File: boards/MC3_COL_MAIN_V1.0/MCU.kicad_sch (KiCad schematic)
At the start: 39 parts, among them J2 SWD, SW1 SKRKAEE020, U10 GP1S094HCZ0F, U2 STM32F412RET6, U9 AEDR-8300-1Q0, Y1 8MHz

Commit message: GP1S094 from datasheet: pins 1=A 2=C 3=E 4=K, THT footprint (4.55x2.0 grid, 1.2mm boss NPTH); R36->100R R37->47k for worst-case CTR; ref collisions fixed (C33->C37, #PWR010-013->#PWR0107-0110)
Co-Authored-By: Claude Fable 5 <noreply@anthropic.com>
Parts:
- R36: value 220R -> 100R; LCSC C25091 -> C25076; Note no COTS record - commodity support part; ~10 mA IR LED from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 -> no COTS record - IR LED drive ~20 mA from +3V3; sized again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
- R37: value 10k -> 47k; LCSC C25744 -> C25792; Note no COTS record - phototransistor pull-up to +3V3 -> no COTS record - collector pull-up sized for worst-case CTR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
- U10: footprint (none) -> MC3_COL_MAIN:GP1S094HCZ0F; Note PROVISIONAL - yaw homing datum, transmissive interrupter, 3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 -> Yaw homing datum, 3 mm slot 0.3 mm aperture. Flag present =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
- renumbered C33 to C37
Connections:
- net GND: now also U10.3 (E); no longer U10.2 (K)
- net YAW_HOME: now also U10.2 (C); no longer U10.3 (C)

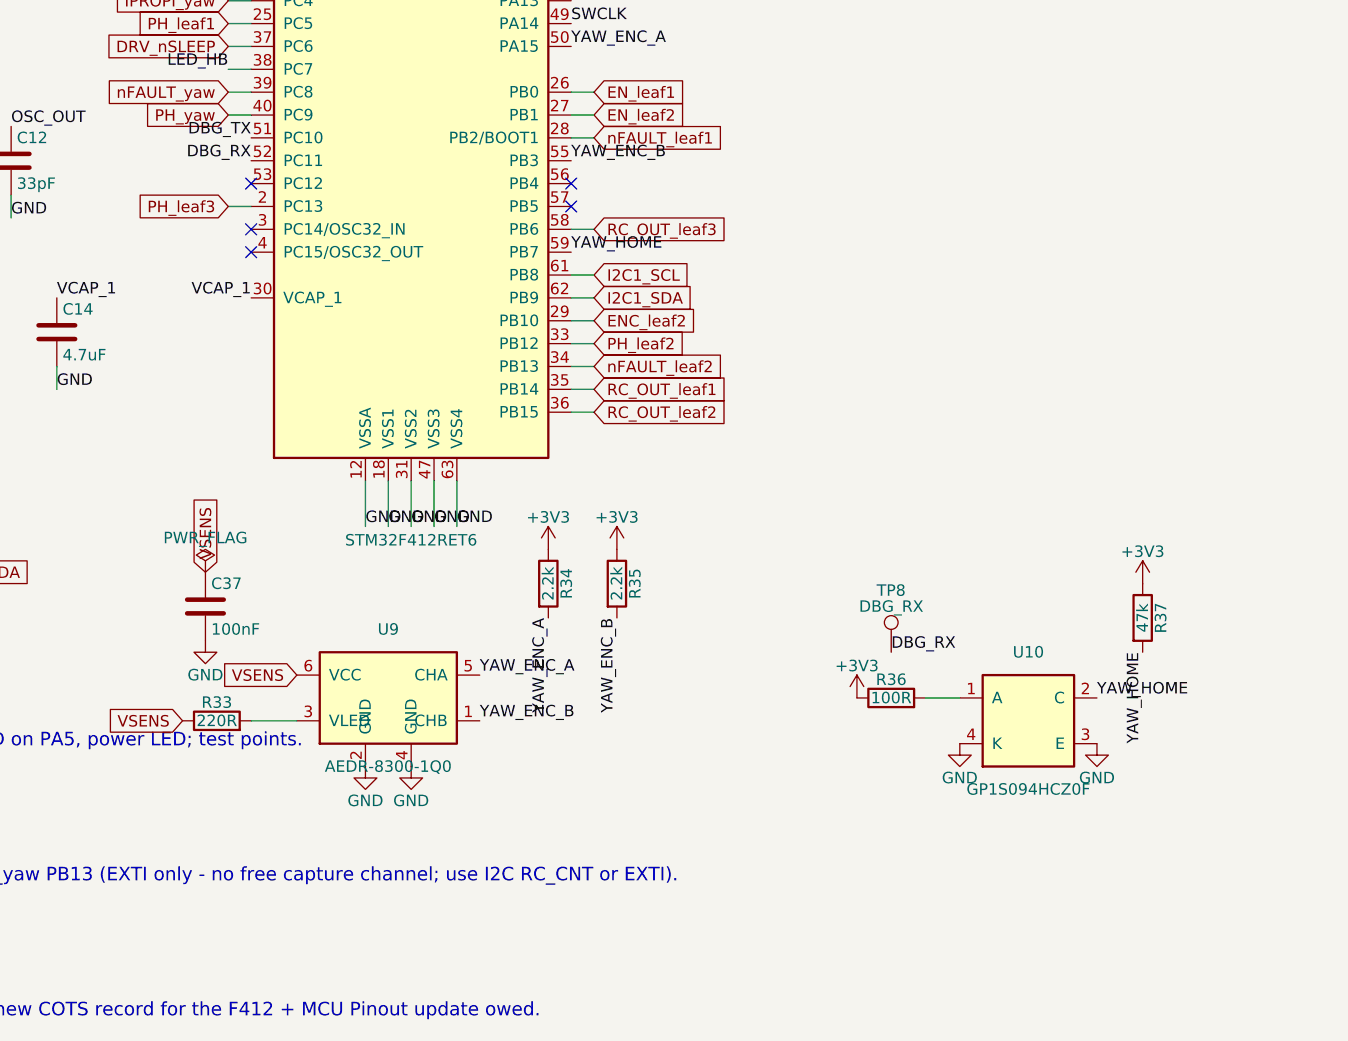
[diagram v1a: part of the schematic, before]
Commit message: Second yaw interrupter U11 (+R38/R39): YAW_LIM on PC12/EXTI, 180 deg from U10 - both hard stops get soft limits; power refs pre-renamed #PWR0111-0114
Co-Authored-By: Claude Fable 5 <noreply@anthropic.com>
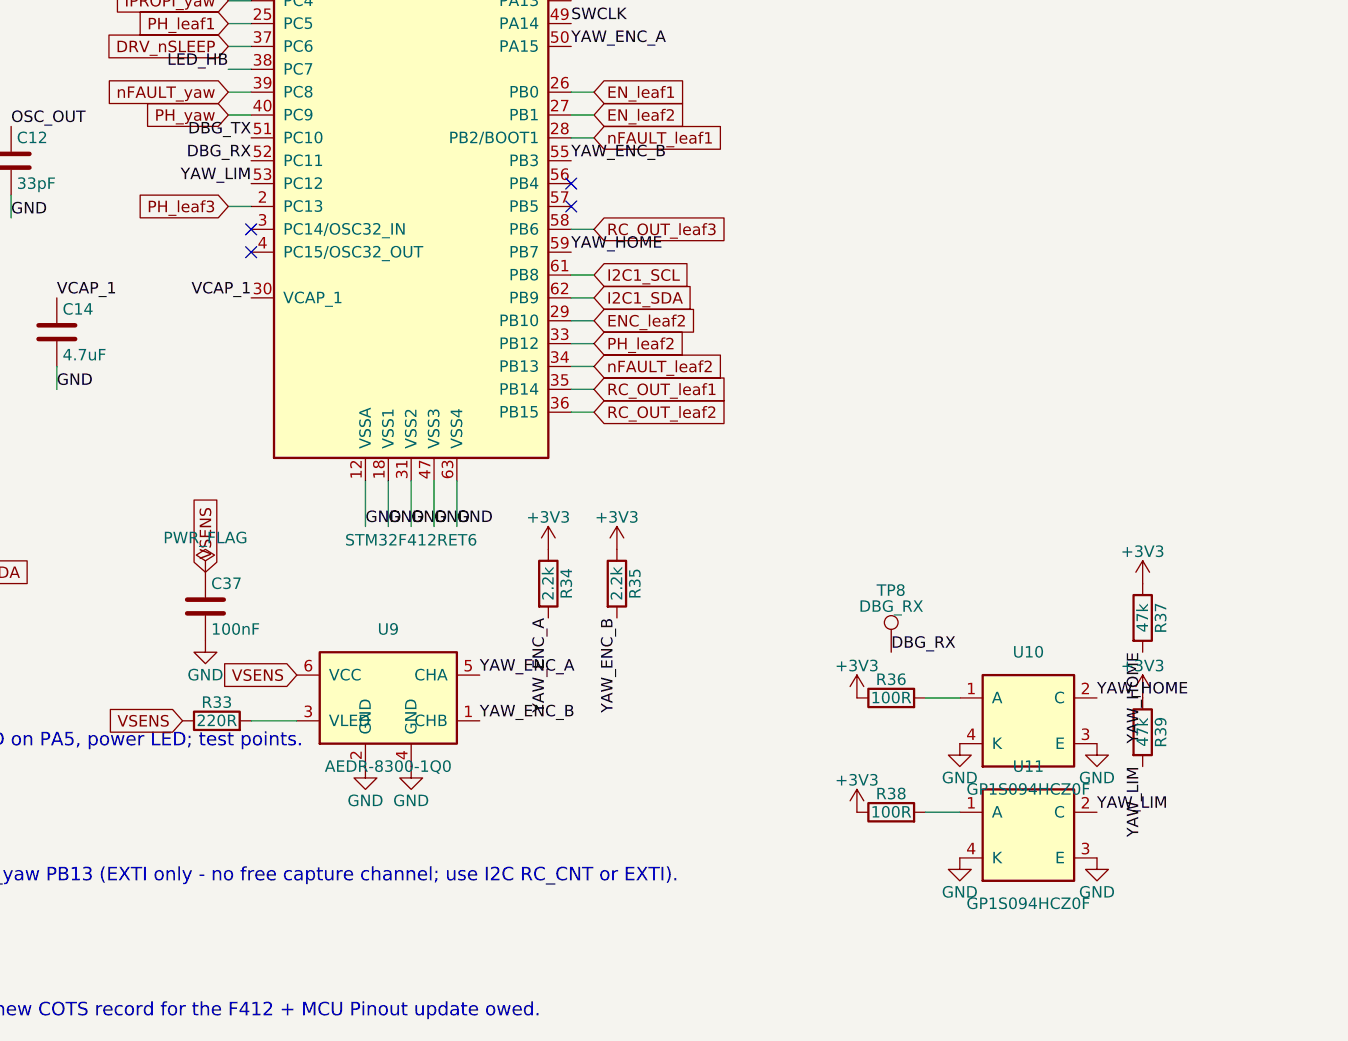
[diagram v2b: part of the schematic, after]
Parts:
- added R38: 100R, MC3_COL_MAIN:R_0402_1005Metric, symbol Device:R
- added R39: 47k, MC3_COL_MAIN:R_0402_1005Metric, symbol Device:R
- added U11: GP1S094HCZ0F, MC3_COL_MAIN:GP1S094HCZ0F, symbol MC3_COL_MAIN:GP1S094HCZ0F
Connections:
- net +3V3: now also R38.1, R39.1
- net GND: now also U11.3 (E), U11.4 (K)
- net YAW_LIM: now reaches U2.53 (PC12)
- net YAW_LIM: now also R39.2, U11.2 (C)
- new net: R38.2, U11.1 (A)
- no-connect marks 6 -> 5

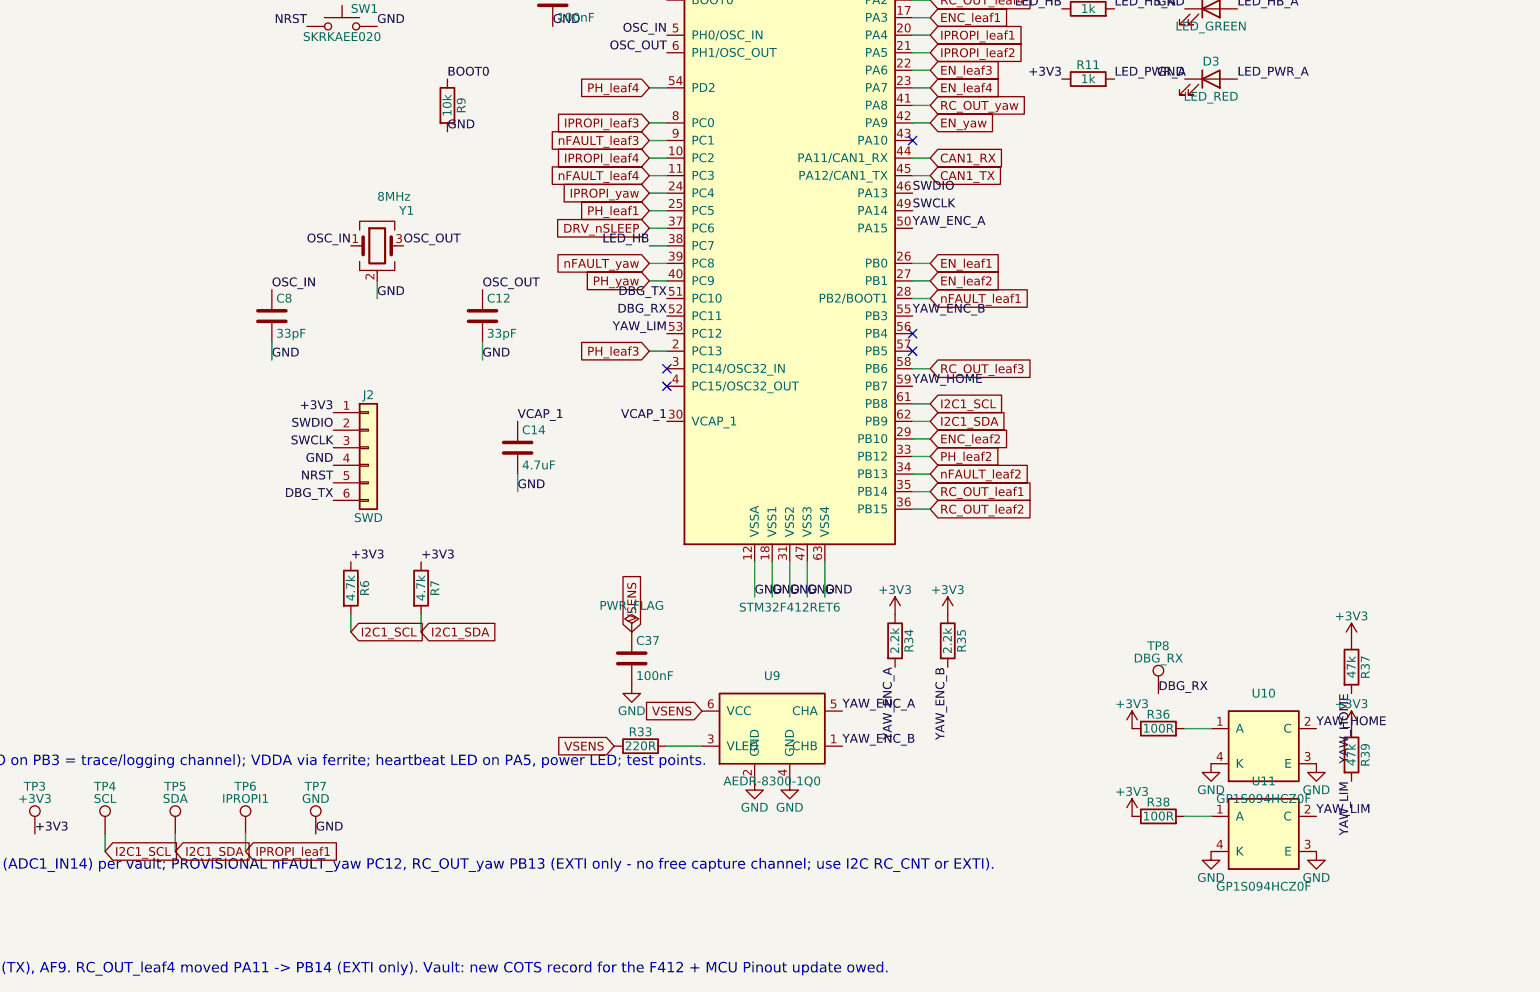
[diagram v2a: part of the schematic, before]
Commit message: Review fixes applied (C21, C37 order, stitching vias) + review-driven adds: 5x 1nF IPROPI ADC filters (C38-42, C1523), U8 VIO 100nF (C43), 3x M2.5 NPTH mounting holes (H1-3) - caps placed unwired, user wires; holes placed in layout by user
Co-Authored-By: Claude Fable 5 <noreply@anthropic.com>
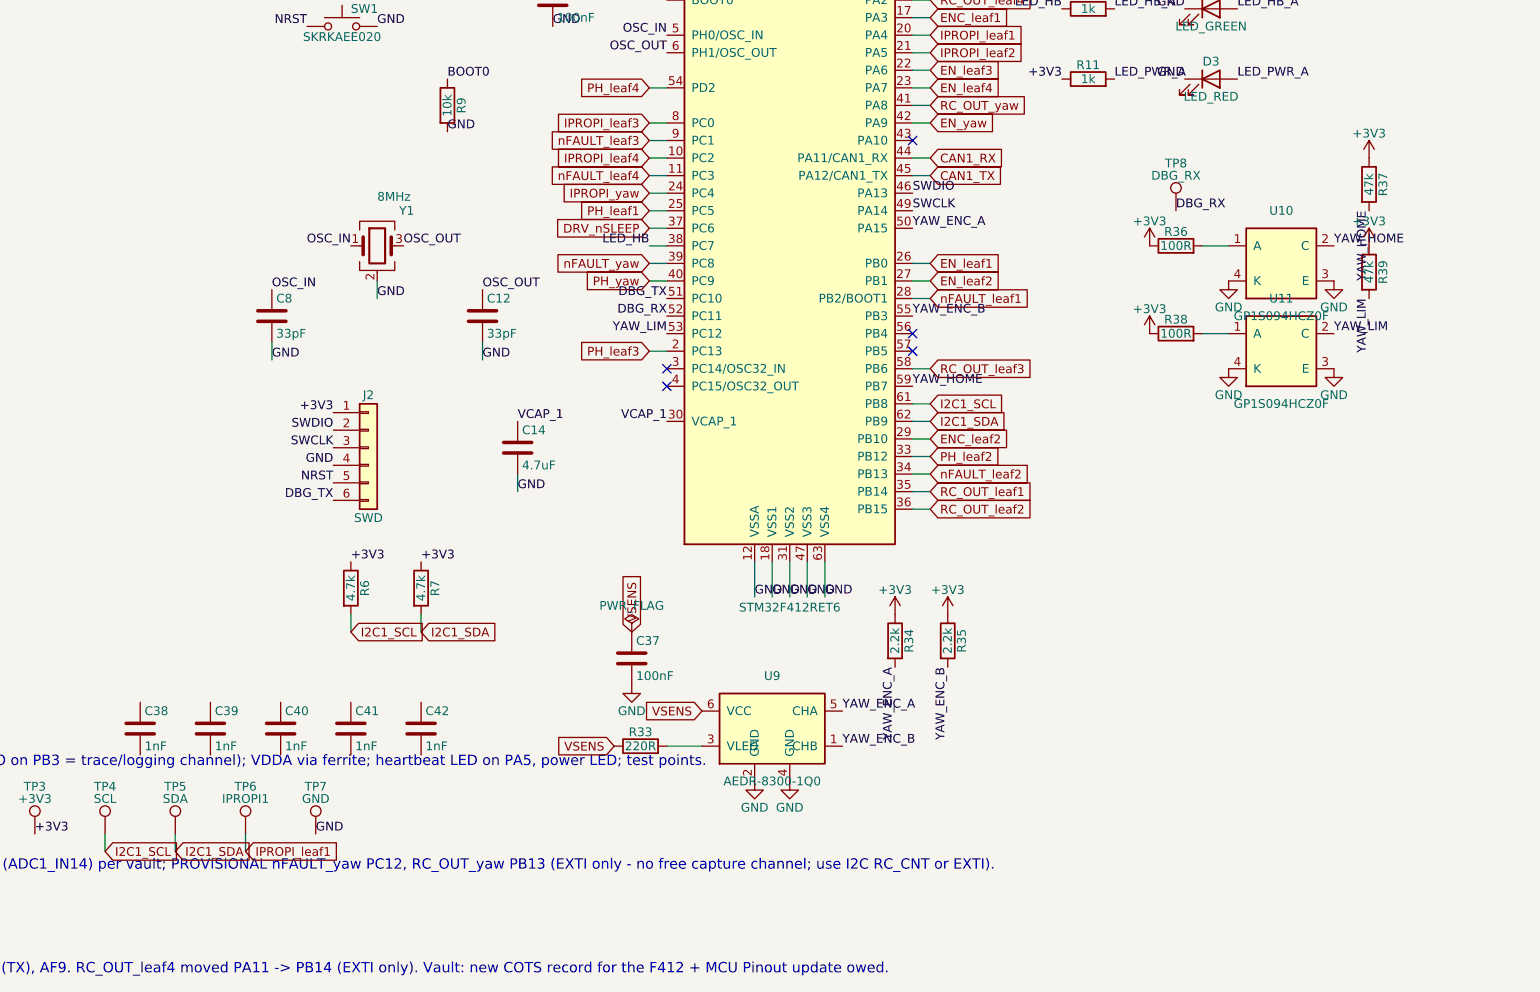
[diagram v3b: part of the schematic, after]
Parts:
- added C38, C39, C40, C41, C42: 1nF, MC3_COL_MAIN:C_0402_1005Metric, symbol Device:C
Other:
- moved on the sheet: R36, R37, R38, R39, TP8, U10, U11

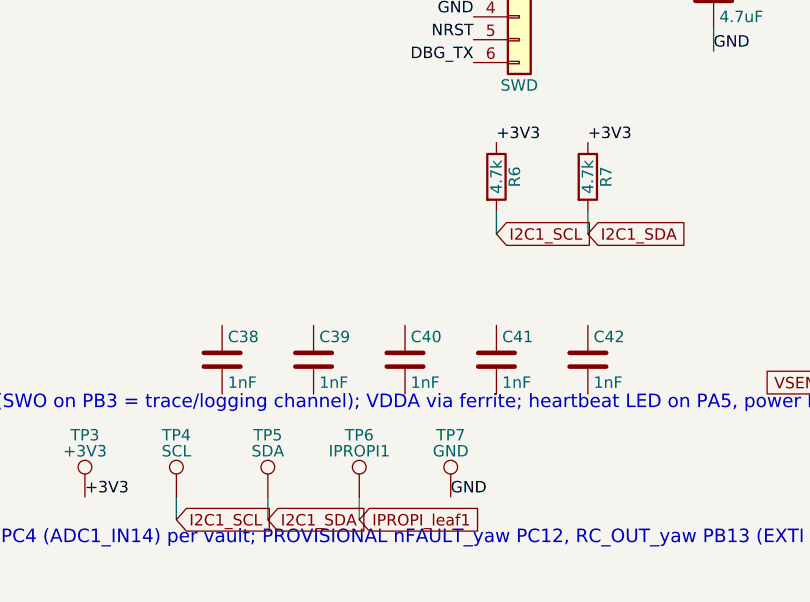
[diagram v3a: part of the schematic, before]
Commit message: Wire the review caps: C38-42 onto IPROPI_* (global labels) + GND, C43 onto +3V3/GND; power refs #PWR0115-0121
Co-Authored-By: Claude Fable 5 <noreply@anthropic.com>
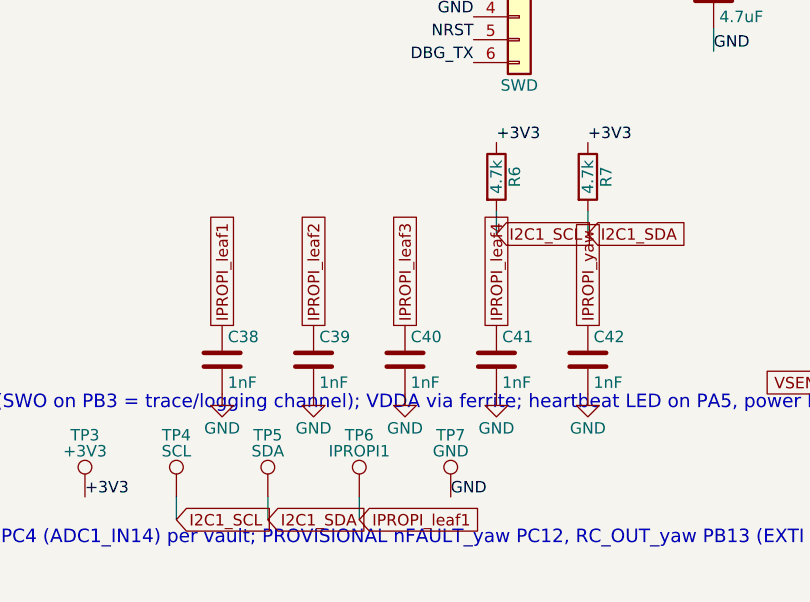
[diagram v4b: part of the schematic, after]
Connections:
- net GND: now also C38.2, C39.2, C40.2, C41.2, C42.2
- net IPROPI_leaf1: now also C38.1
- net IPROPI_leaf2: now also C39.1
- net IPROPI_leaf3: now also C40.1
- net IPROPI_leaf4: now also C41.1
- net IPROPI_yaw: now also C42.1
